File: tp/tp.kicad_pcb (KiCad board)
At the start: 2 copper layers, 73 x 22 mm, 22 parts, among them J1 Conn_01x02, J2 Conn_01x04, T1 ZMPT101B, U1 LM358

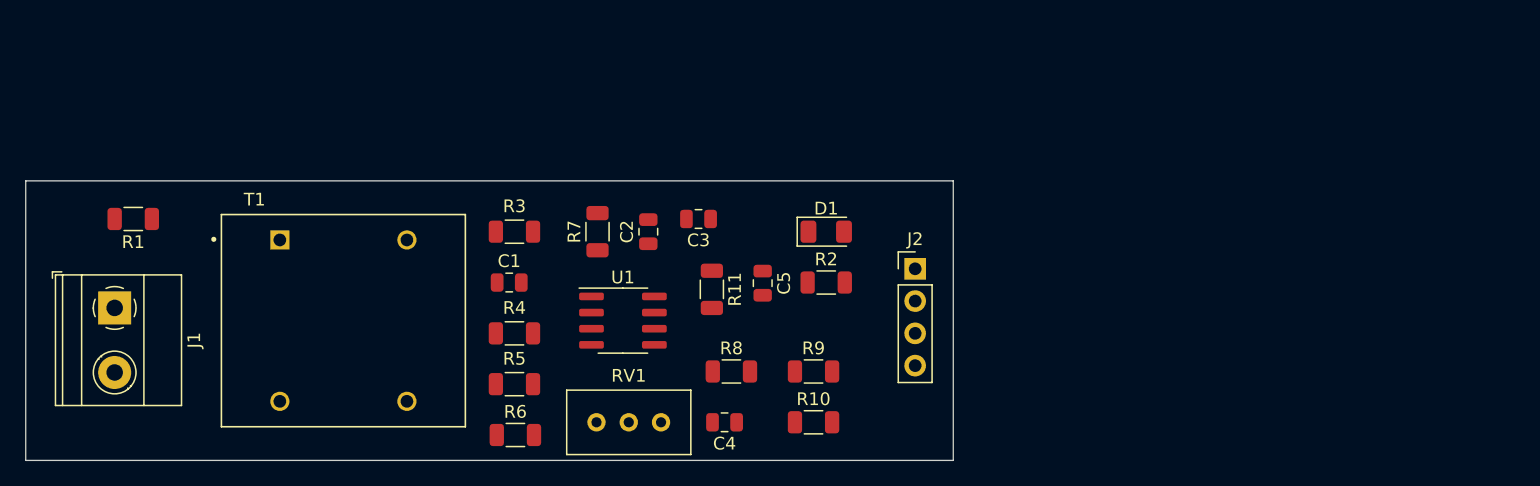
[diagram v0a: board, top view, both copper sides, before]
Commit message: Avance de PCB. Agregado de agujeros de fijacion
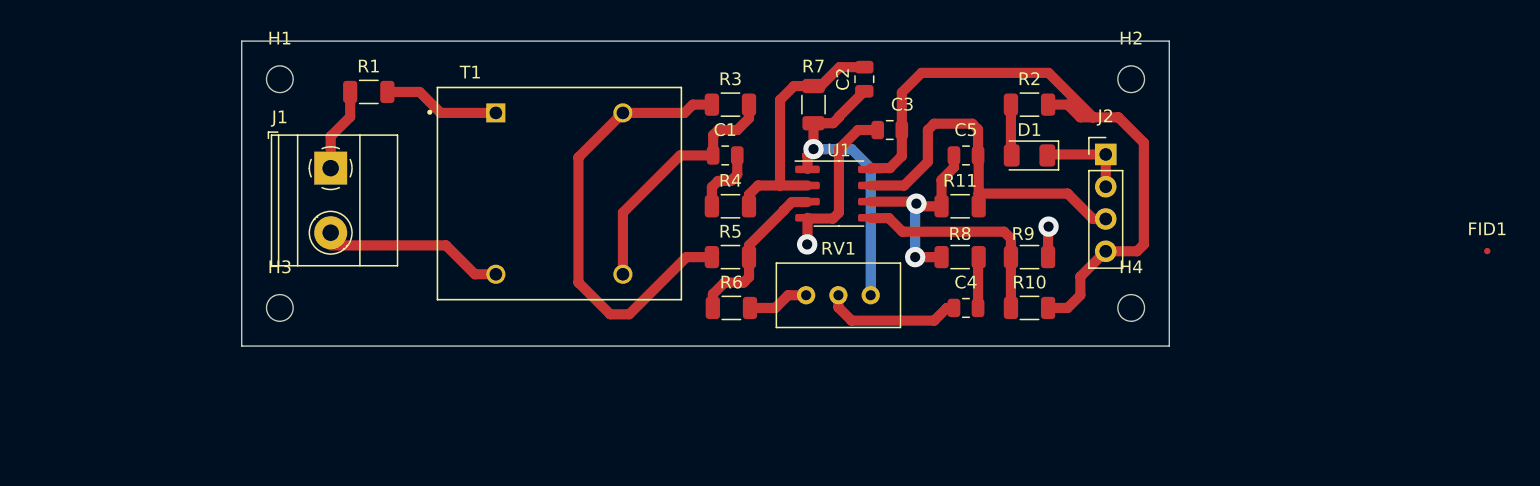
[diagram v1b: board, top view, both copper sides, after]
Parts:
- added FID1: Fiducial, Fiducial:Fiducial_0.5mm_Mask1.5mm, F.Cu at (210.0, 103.5)
- added H1: MountingHole, MountingHole:MountingHole_2.1mm, F.Cu at (115.0, 90.0)
- added H2: MountingHole, MountingHole:MountingHole_2.1mm, F.Cu at (182.0, 90.0)
- added H3: MountingHole, MountingHole:MountingHole_2.1mm, F.Cu at (115.0, 108.0)
- added H4: MountingHole, MountingHole:MountingHole_2.1mm, F.Cu at (182.0, 108.0)
- moved R2 21.3 mm to (174.0, 92.0), turned to 180 degrees
- moved R1 21.1 mm to (122.0, 91.0)
- moved C4 21.0 mm to (169.0, 108.0)
- moved C2 20.8 mm to (161.0, 90.0)
- moved R11 20.6 mm to (168.5, 100.0), turned to 180 degrees
- moved J1 20.2 mm to (119.0, 97.0)
- moved R8 20.1 mm to (168.5, 104.0)
- moved C1 19.7 mm to (150.1, 96.0), turned to 180 degrees
- moved R3 19.7 mm to (150.5, 92.0)
- moved R4 19.7 mm to (150.5, 100.0)
- moved R5 19.7 mm to (150.5, 104.0)
- moved R6 19.7 mm to (150.5, 108.0), turned to 180 degrees
- moved R7 19.7 mm to (157.0, 92.0)
- moved T1 19.7 mm to (137.0, 99.0)
- moved U1 19.7 mm to (159.0, 99.0)
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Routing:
- net +5V: track 0.00 -> 52.3 mm
- net Net-(R3-Pad2): track 0.00 -> 35.5 mm
- net /OUT: track 0.00 -> 29.0 mm
- net GND: track 0.00 -> 28.0 mm, vias 0 -> 2
- net Net-(C2-Pad1): track 0.00 -> 25.0 mm, vias 0 -> 1
- net Net-(C2-Pad2): track 0.00 -> 20.3 mm
- net Net-(C1-Pad2): track 0.00 -> 19.9 mm
- net Net-(R10-Pad2): track 0.00 -> 18.2 mm
- net Net-(C5-Pad2): track 0.00 -> 17.0 mm, vias 0 -> 2
- net Net-(J1-Pad2): track 0.00 -> 13.9 mm
- net Net-(R5-Pad1): track 0.00 -> 13.0 mm
- net Net-(C4-Pad2): track 0.00 -> 10.9 mm
- net Net-(R1-Pad1): track 0.00 -> 9.22 mm
- net Net-(J1-Pad1): track 0.00 -> 6.64 mm
- net Net-(C1-Pad1): track 0.00 -> 5.41 mm
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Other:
- board size 73 x 22 mm -> 73 x 24 mm
- net class Default: clearance 0.8 -> 0.5
- rule trace_clearance: 0.8 -> 0.5

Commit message: Se aplicaron todos los comentarios hechos en la revisión del docente
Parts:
- C1, C4: value 1u -> 1uF
- C2, C3, C5: value 1n -> 1nF
- D1: value LED_ALT -> SMD Red Led
- R1, R10, R11, R2, R3, R4, R5, R6, R7, R8, R9: footprint Resistor_SMD:R_1206_3216Metric -> Resistor_SMD:R_0805_2012Metric
- moved C1 2.00 mm to (150.1, 94.0)
- moved R3 2.00 mm to (150.5, 90.0)
- moved R4 2.00 mm to (150.5, 98.0)
- moved R5 2.00 mm to (150.5, 102.0)
- moved R6 2.00 mm to (150.5, 106.0)
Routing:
- net Net-(R5-Pad1): track 13.0 -> 0.00 mm
- net GND: track 28.0 -> 23.2 mm
- net Net-(C2-Pad2): track 20.3 -> 16.6 mm
- net Net-(R3-Pad2): track 35.5 -> 32.0 mm
- net Net-(C1-Pad1): track 5.41 -> 2.21 mm
- net Net-(C1-Pad2): track 19.9 -> 17.5 mm

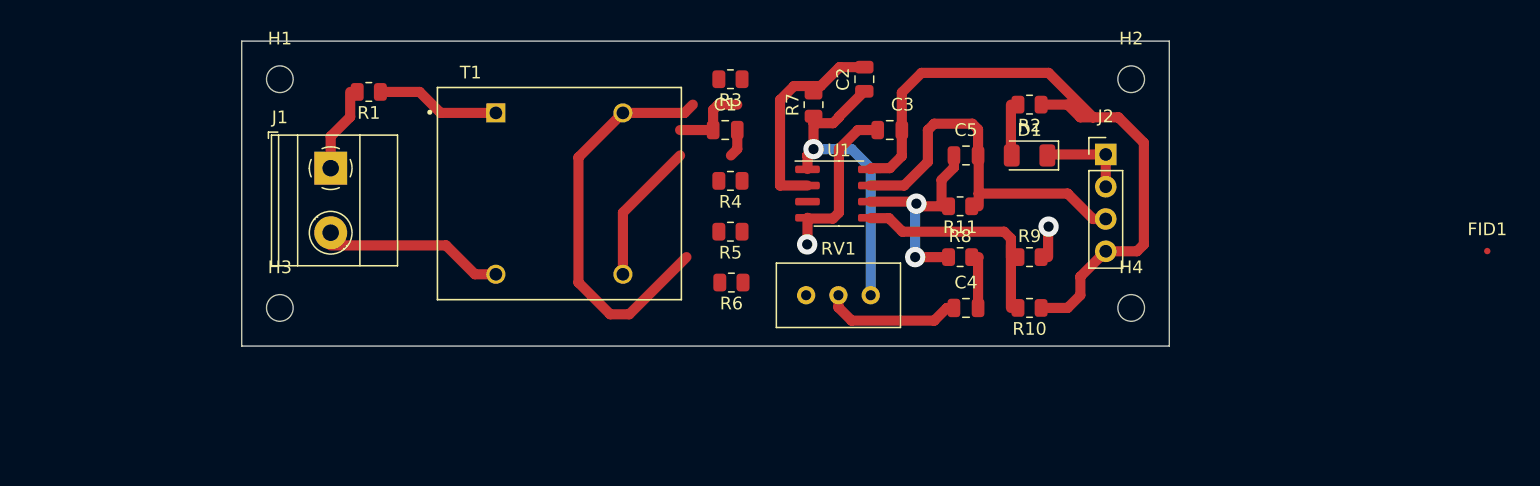
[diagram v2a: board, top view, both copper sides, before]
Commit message: PCB Finalizado
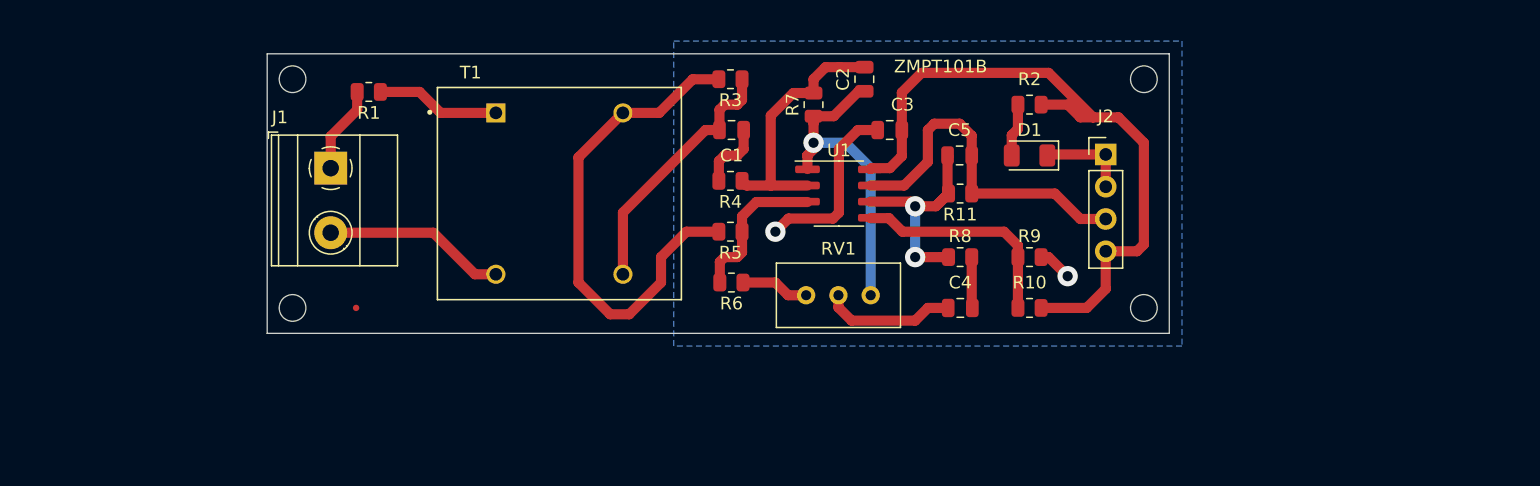
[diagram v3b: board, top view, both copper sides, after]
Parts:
- moved FID1 89.1 mm to (121.0, 108.0)
- moved H1 1.00 mm to (116.0, 90.0)
- moved H2 1.00 mm to (183.0, 90.0)
- moved H3 1.00 mm to (116.0, 108.0)
- moved H4 1.00 mm to (183.0, 108.0)
- moved R11 1.00 mm to (168.5, 99.0)
- moved C1 0.50 mm to (150.6, 94.0)
- moved C5 0.50 mm to (168.5, 96.0)
- moved C4 0.45 mm to (168.6, 108.0)
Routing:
- net Net-(R5-Pad1): track 0.00 -> 12.1 mm
- net Net-(R3-Pad2): track 32.0 -> 39.4 mm
- net GND: track 23.2 -> 29.6 mm
- net Net-(C2-Pad2): track 16.6 -> 20.4 mm
- net Net-(C1-Pad1): track 2.21 -> 5.39 mm
- net Net-(C1-Pad2): track 17.5 -> 20.5 mm
- net +5V: track 52.3 -> 54.3 mm
- net /OUT: track 29.0 -> 27.8 mm
- net Net-(R10-Pad2): track 18.2 -> 17.4 mm
- net Net-(C5-Pad2): track 17.0 -> 17.6 mm
- net Net-(R1-Pad1): track 9.22 -> 9.77 mm
- added copper zone on B.Cu, net GND
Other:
- board size 73 x 24 mm -> 71 x 22 mm
- net class Default: clearance 0.5 -> 0.3
- rule trace_clearance: 0.5 -> 0.3
- board text added: "GND"
- board text added: "IND. ARGENTINA"
- board text added: "L"
- board text added: "Mínimos: Grillas: 1 mm / 0,5 mm Vía: 1,6 mm / 0.8 mm Pista: 0,8 mm Dist. a borde: 0,3 mm Terminación: HASL"
- board text added: "N"
- board text added: "OUT"
- board text added: "VCC"
- board text added: "ZMPT101B"

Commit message: Proyecto actualizado según revisión  F. Calcavecchia 18/04/2021
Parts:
- added FID2: Fiducial, Fiducial:Fiducial_0.5mm_Mask1.5mm, F.Cu at (179.0, 90.0)
- moved FID1 1.50 mm to (119.5, 108.0)
- moved C2 0.50 mm to (161.0, 90.5)
- moved J1 0.50 mm to (119.5, 97.0)
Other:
- board text added: "Mínimos: Grillas: 1 mm / 0,5 mm Margen: 0,3 mm Vía: 1,6 mm / 0.8 mm Pista: 0,8 mm Dist. a borde: 0,3 mm Terminación: HASL"
- board text added: "ZMPT101B-V1"
- board text removed: "L"
- board text removed: "Mínimos: Grillas: 1 mm / 0,5 mm Vía: 1,6 mm / 0.8 mm Pista: 0,8 mm Dist. a borde: 0,3 mm Terminación: HASL"
- board text removed: "N"
- board text removed: "ZMPT101B"

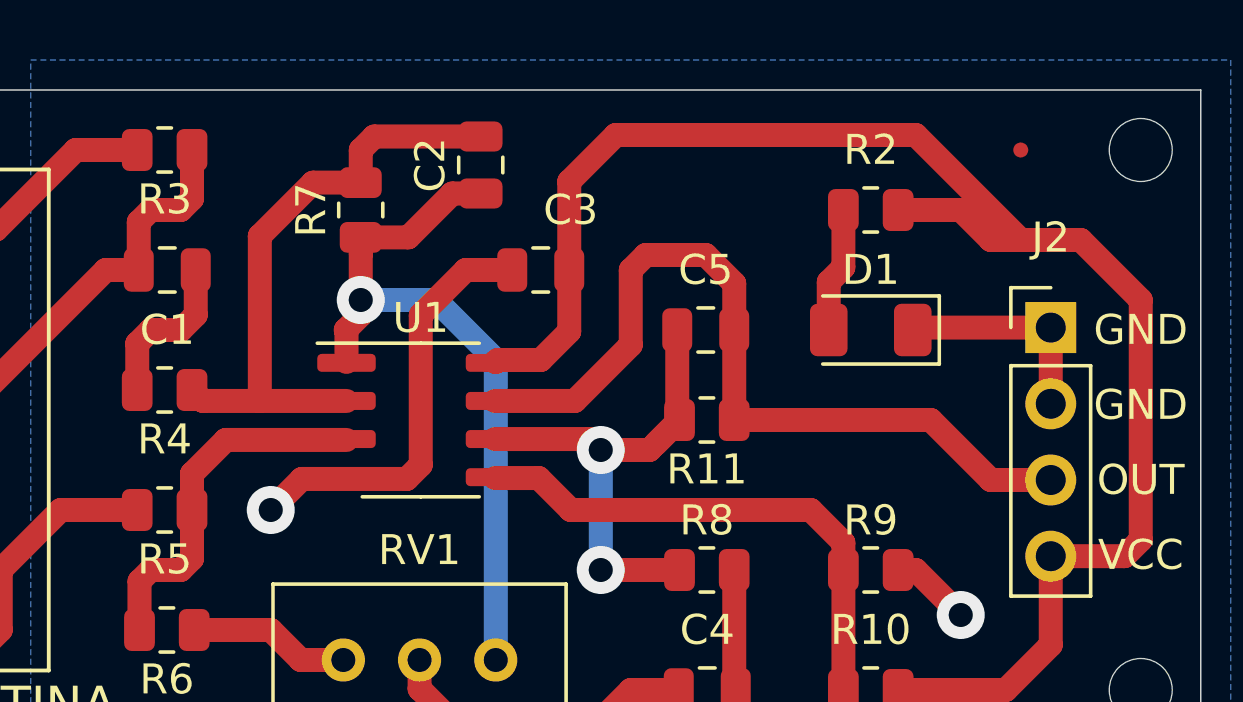
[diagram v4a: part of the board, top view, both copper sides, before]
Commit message: Actualizado segun revision PCB docente
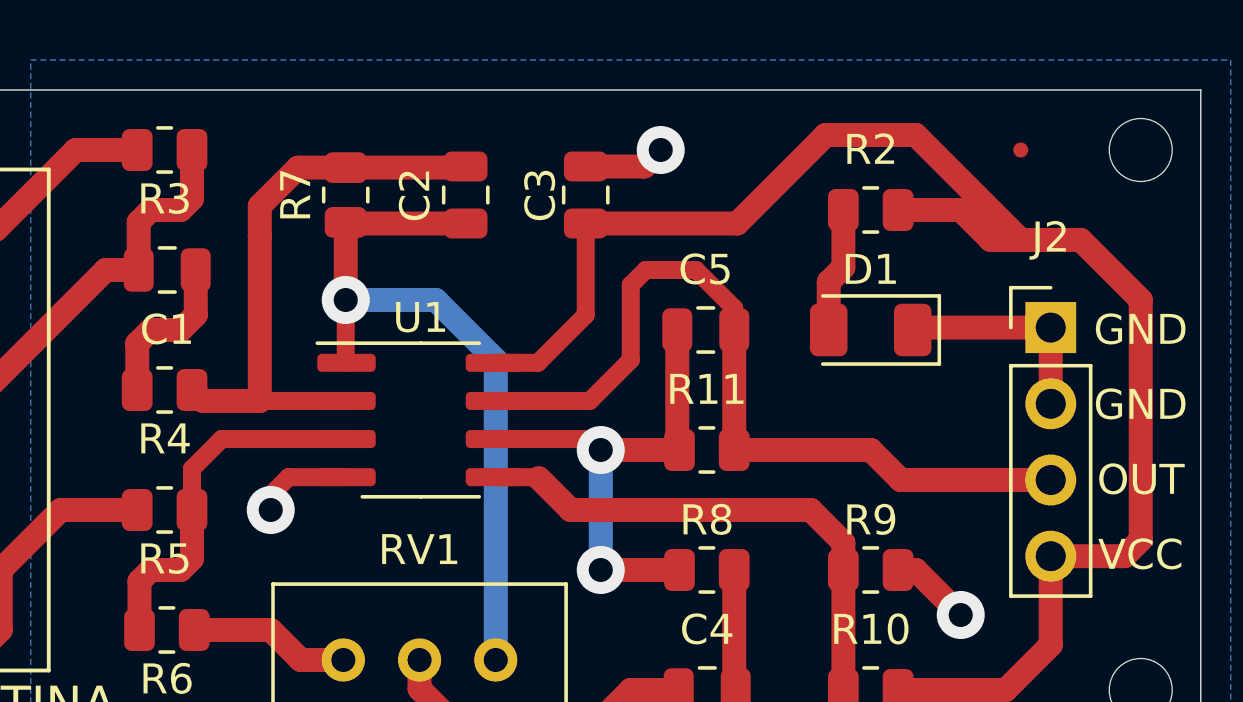
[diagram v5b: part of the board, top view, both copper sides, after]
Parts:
- moved C3 2.92 mm to (164.5, 91.5), turned to 90 degrees
- moved C2 1.12 mm to (160.5, 91.5)
- moved R11 1.00 mm to (168.5, 100.0)
- moved R7 0.71 mm to (156.5, 91.5)
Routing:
- net GND: track 29.6 -> 21.3 mm, vias 2 -> 3
- net +5V: track 54.3 -> 53.1 mm
- net Net-(C2-Pad2): track 20.2 -> 19.2 mm
- net Net-(C5-Pad2): track 17.6 -> 17.1 mm
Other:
- board text added: "Mínimos (Mayer 10 mils): Grillas: 1 mm / 0,5 mm Margen: 0,5 mm Vía: 1,6 mm / 0,8 mm Pista: 0,8 mm / 0,6 mm Dist. a borde: 0,5 mm Terminación: HASL"
- board text removed: "Mínimos: Grillas: 1 mm / 0,5 mm Margen: 0,3 mm Vía: 1,6 mm / 0.8 mm Pista: 0,8 mm Dist. a borde: 0,3 mm Terminación: HASL"
